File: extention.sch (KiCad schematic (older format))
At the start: 16 parts, among them J10 S_1P1T, J8 S_1P1T, J9 S_1P1T, Q1 2N7002, Q2 2N7002, U5 HS0038B, U6 HLT1160

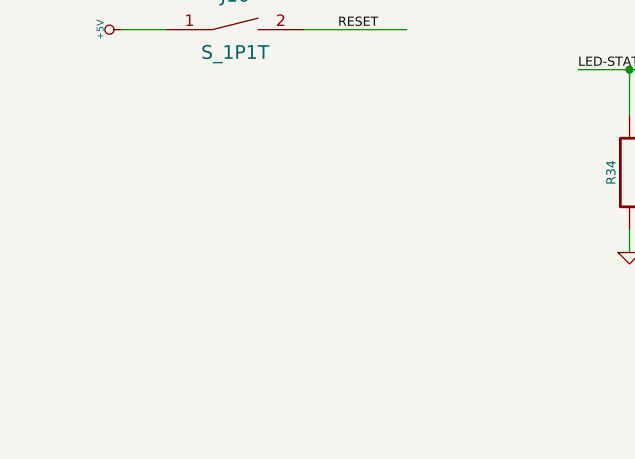
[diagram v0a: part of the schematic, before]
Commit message: 1.4
Fix some issues
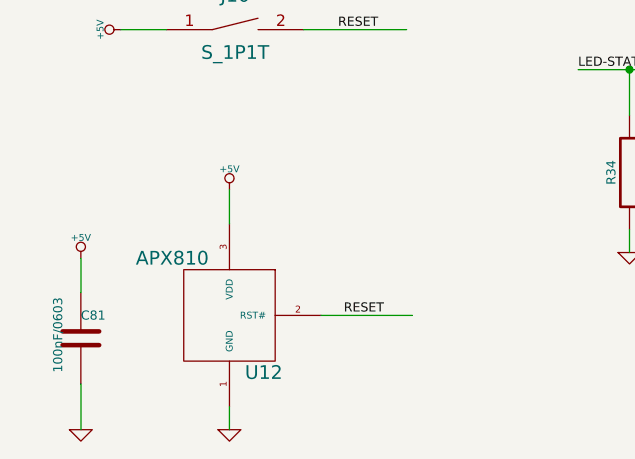
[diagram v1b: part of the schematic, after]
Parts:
- added C81: 100nF/0603, ~, symbol C
- added U12: APX810, ~, symbol APX810
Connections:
- wire segments 48 -> 53
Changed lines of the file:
@@
 Sheet 8 11
 Title ""
-Date "19 sep 2014"
+Date "25 nov 2014"
 Rev ""
 Comp ""
@@
 $EndComp
 $Comp
-L +3.3V #PWR0105
+L +3.3V #PWR0124
 U 1 1 53DE8C79
 P 3400 1600
-F 0 "#PWR0105" H 3400 1560 30  0001 C CNN
+F 0 "#PWR0124" H 3400 1560 30  0001 C CNN
 F 1 "+3.3V" H 3400 1710 30  0000 C CNN
 F 2 "" H 3400 1600 60  0000 C CNN
@@
 $EndComp
 $Comp
-L GND #PWR0106
+L GND #PWR0125
 U 1 1 53DE8C88
 P 2475 2700
-F 0 "#PWR0106" H 2475 2700 30  0001 C CNN
+F 0 "#PWR0125" H 2475 2700 30  0001 C CNN
 F 1 "GND" H 2475 2630 30  0001 C CNN
 F 2 "" H 2475 2700 60  0000 C CNN
@@
 $EndComp
 $Comp
-L GND #PWR0107
+L GND #PWR0126
 U 1 1 53DE8C95
 P 2250 2700
-F 0 "#PWR0107" H 2250 2700 30  0001 C CNN
+F 0 "#PWR0126" H 2250 2700 30  0001 C CNN
 F 1 "GND" H 2250 2630 30  0001 C CNN
 F 2 "" H 2250 2700 60  0000 C CNN
@@
 $EndComp
 $Comp
-L +3.3V #PWR0108
+L +3.3V #PWR0127
 U 1 1 53DE8CF8
 P 5100 1775
-F 0 "#PWR0108" H 5100 1735 30  0001 C CNN
+F 0 "#PWR0127" H 5100 1735 30  0001 C CNN
 F 1 "+3.3V" H 5100 1885 30  0000 C CNN
 F 2 "" H 5100 1775 60  0000 C CNN
@@
 $EndComp
 $Comp
-L GND #PWR0109
+L GND #PWR0128
 U 1 1 53DE8CFE
 P 4875 2600
-F 0 "#PWR0109" H 4875 2600 30  0001 C CNN
+F 0 "#PWR0128" H 4875 2600 30  0001 C CNN
 F 1 "GND" H 4875 2530 30  0001 C CNN
 F 2 "" H 4875 2600 60  0000 C CNN
@@
 $EndComp
 $Comp
-L GND #PWR0110
+L GND #PWR0129
 U 1 1 53DE8D1E
 P 5100 2600
-F 0 "#PWR0110" H 5100 2600 30  0001 C CNN
+F 0 "#PWR0129" H 5100 2600 30  0001 C CNN
 F 1 "GND" H 5100 2530 30  0001 C CNN
 F 2 "" H 5100 2600 60  0000 C CNN
@@
 $EndComp
 $Comp
-L GND #PWR0111
+L GND #PWR0130
 U 1 1 53DB6C74
 P 1975 4100
-F 0 "#PWR0111" H 1975 4100 30  0001 C CNN
+F 0 "#PWR0130" H 1975 4100 30  0001 C CNN
 F 1 "GND" H 1975 4030 30  0001 C CNN
 F 2 "" H 1975 4100 60  0000 C CNN
@@
 $EndComp
 $Comp
-L GND #PWR0112
+L GND #PWR0131
 U 1 1 53DB6CA1
 P 1975 4450
-F 0 "#PWR0112" H 1975 4450 30  0001 C CNN
+F 0 "#PWR0131" H 1975 4450 30  0001 C CNN
 F 1 "GND" H 1975 4380 30  0001 C CNN
 F 2 "" H 1975 4450 60  0000 C CNN
@@
 $EndComp
 $Comp
-L +3.3V #PWR0113
+L +3.3V #PWR0132
 U 1 1 53DB6F84
 P 5175 3475
-F 0 "#PWR0113" H 5175 3435 30  0001 C CNN
+F 0 "#PWR0132" H 5175 3435 30  0001 C CNN
 F 1 "+3.3V" H 5175 3585 30  0000 C CNN
 F 2 "" H 5175 3475 60  0000 C CNN
@@
 $EndComp
 $Comp
-L GND #PWR0114
+L GND #PWR0133
 U 1 1 53DB72A6
 P 4200 5775
-F 0 "#PWR0114" H 4200 5775 30  0001 C CNN
+F 0 "#PWR0133" H 4200 5775 30  0001 C CNN
 F 1 "GND" H 4200 5705 30  0001 C CNN
 F 2 "" H 4200 5775 60  0000 C CNN
@@
 $EndComp
 $Comp
-L GND #PWR0115
+L GND #PWR0134
 U 1 1 53DB72B8
 P 5250 5775
-F 0 "#PWR0115" H 5250 5775 30  0001 C CNN
+F 0 "#PWR0134" H 5250 5775 30  0001 C CNN
 F 1 "GND" H 5250 5705 30  0001 C CNN
 F 2 "" H 5250 5775 60  0000 C CNN
@@
 $EndComp
 $Comp
-L GND #PWR0116
+L GND #PWR0135
 U 1 1 53DB72BE
 P 4700 5775
-F 0 "#PWR0116" H 4700 5775 30  0001 C CNN
+F 0 "#PWR0135" H 4700 5775 30  0001 C CNN
 F 1 "GND" H 4700 5705 30  0001 C CNN
 F 2 "" H 4700 5775 60  0000 C CNN
@@
 $EndComp
 $Comp
-L GND #PWR0117
+L GND #PWR0136
 U 1 1 53DB72C4
 P 5700 5775
-F 0 "#PWR0117" H 5700 5775 30  0001 C CNN
+F 0 "#PWR0136" H 5700 5775 30  0001 C CNN
 F 1 "GND" H 5700 5705 30  0001 C CNN
 F 2 "" H 5700 5775 60  0000 C CNN
@@
 3V3
 $Comp
-L +3.3V #PWR0118
+L +3.3V #PWR0137
 U 1 1 53DB7765
 P 7300 1650
-F 0 "#PWR0118" H 7300 1610 30  0001 C CNN
+F 0 "#PWR0137" H 7300 1610 30  0001 C CNN
 F 1 "+3.3V" H 7300 1760 30  0000 C CNN
 F 2 "" H 7300 1650 60  0000 C CNN
@@
 $EndComp
 $Comp
-L GND #PWR0119
+L GND #PWR0138
 U 1 1 53DB776B
 P 7300 1875
-F 0 "#PWR0119" H 7300 1875 30  0001 C CNN
+F 0 "#PWR0138" H 7300 1875 30  0001 C CNN
 F 1 "GND" H 7300 1805 30  0001 C CNN
 F 2 "" H 7300 1875 60  0000 C CNN
@@
 LED-STATUS1
 $Comp
-L +5V #PWR0120
+L +5V #PWR0139
 U 1 1 53F3AFA9
 P 1975 4800
-F 0 "#PWR0120" H 1975 4890 20  0001 C CNN
+F 0 "#PWR0139" H 1975 4890 20  0001 C CNN
 F 1 "+5V" H 1975 4890 30  0000 C CNN
 F 2 "" H 1975 4800 60  0000 C CNN
@@
 $EndComp
 $Comp
-L +5V #PWR0121
+L +5V #PWR0140
 U 1 1 53F3AFC0
 P 7300 1475
-F 0 "#PWR0121" H 7300 1565 20  0001 C CNN
+F 0 "#PWR0140" H 7300 1565 20  0001 C CNN
 F 1 "+5V" H 7300 1565 30  0000 C CNN
 F 2 "" H 7300 1475 60  0000 C CNN
@@
 Wire Wire Line
 	7300 1475 6775 1475
+$Comp
+L APX810 U12
+U 1 1 546B3053
+P 2450 6050
+F 0 "U12" H 2600 5800 60  0000 C CNN
+F 1 "APX810" H 2200 6300 60  0000 C CNN
+F 2 "~" H 2450 6050 60  0000 C CNN
+F 3 "~" H 2450 6050 60  0000 C CNN
+	1    2450 6050
+	1    0    0    -1
+$EndComp
+$Comp
+L +5V #PWR0141
+U 1 1 546B306A
+P 2450 5500
+F 0 "#PWR0141" H 2450 5590 20  0001 C CNN
+F 1 "+5V" H 2450 5590 30  0000 C CNN
+F 2 "" H 2450 5500 60  0000 C CNN
+F 3 "" H 2450 5500 60  0000 C CNN
+	1    2450 5500
+	1    0    0    -1
+$EndComp
+$Comp
+L +5V #PWR0142
+U 1 1 546B3070
+P 1800 5800
+F 0 "#PWR0142" H 1800 5890 20  0001 C CNN
+F 1 "+5V" H 1800 5890 30  0000 C CNN
+F 2 "" H 1800 5800 60  0000 C CNN
+F 3 "" H 1800 5800 60  0000 C CNN
+	1    1800 5800
+	1    0    0    -1
+$EndComp
+$Comp
+L C C81
+U 1 1 546B3076
+P 1800 6150
+F 0 "C81" H 1800 6250 40  0000 L CNN
+F 1 "100nF/0603" V 1700 6000 40  0000 L CNN
+F 2 "~" H 1838 6000 30  0000 C CNN
+F 3 "~" H 1800 6150 60  0000 C CNN
+	1    1800 6150
+	1    0    0    -1
+$EndComp
+$Comp
+L GND #PWR0143
+U 1 1 546B3088
+P 1800 6550
+F 0 "#PWR0143" H 1800 6550 30  0001 C CNN
+F 1 "GND" H 1800 6480 30  0001 C CNN
+F 2 "" H 1800 6550 60  0000 C CNN
+F 3 "" H 1800 6550 60  0000 C CNN
+	1    1800 6550
+	1    0    0    -1
+$EndComp
+$Comp
+L GND #PWR0144
+U 1 1 546B308E
+P 2450 6550
+F 0 "#PWR0144" H 2450 6550 30  0001 C CNN
+F 1 "GND" H 2450 6480 30  0001 C CNN
+F 2 "" H 2450 6550 60  0000 C CNN
+F 3 "" H 2450 6550 60  0000 C CNN
+	1    2450 6550
+	1    0    0    -1
+$EndComp
+Wire Wire Line
+	1800 5950 1800 5800
+Wire Wire Line
+	1800 6350 1800 6550
+Wire Wire Line
+	2450 6450 2450 6550
+Wire Wire Line
+	2450 5650 2450 5500
+Wire Wire Line
+	2850 6050 3250 6050
+Text Label 2950 6050 0    40   ~ 0
+RESET
 $EndSCHEMATC
